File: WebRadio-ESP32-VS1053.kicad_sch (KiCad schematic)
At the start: 75 parts, among them J1 Conn_01x02, J2 JST PH 2mm, J3 JST PH 2mm, J4 AudioJack3, J5 Conn_01x02_Pin, J6 JST PH 2mm, P1 USB_C_Plug_USB2.0, SW1 SW_Push, SW2 SW_Push, SW3 SW_Push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

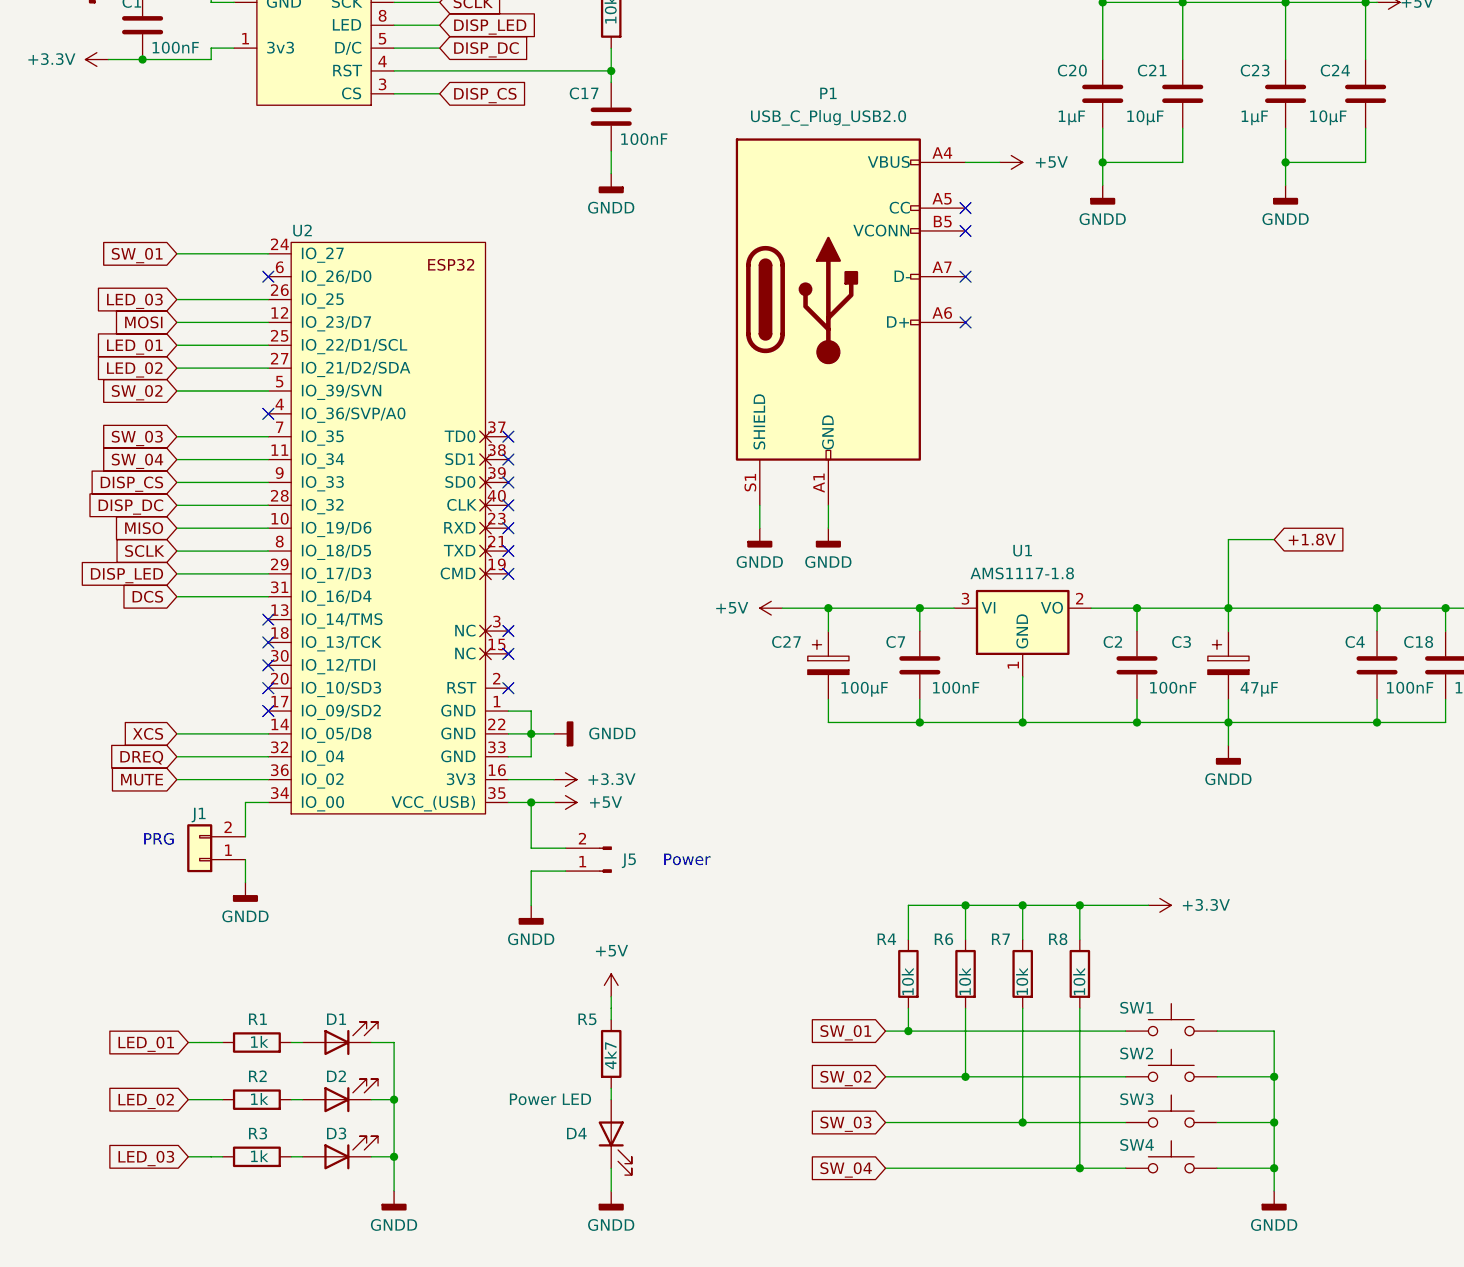
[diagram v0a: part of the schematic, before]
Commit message: add pin header for leds and swiches
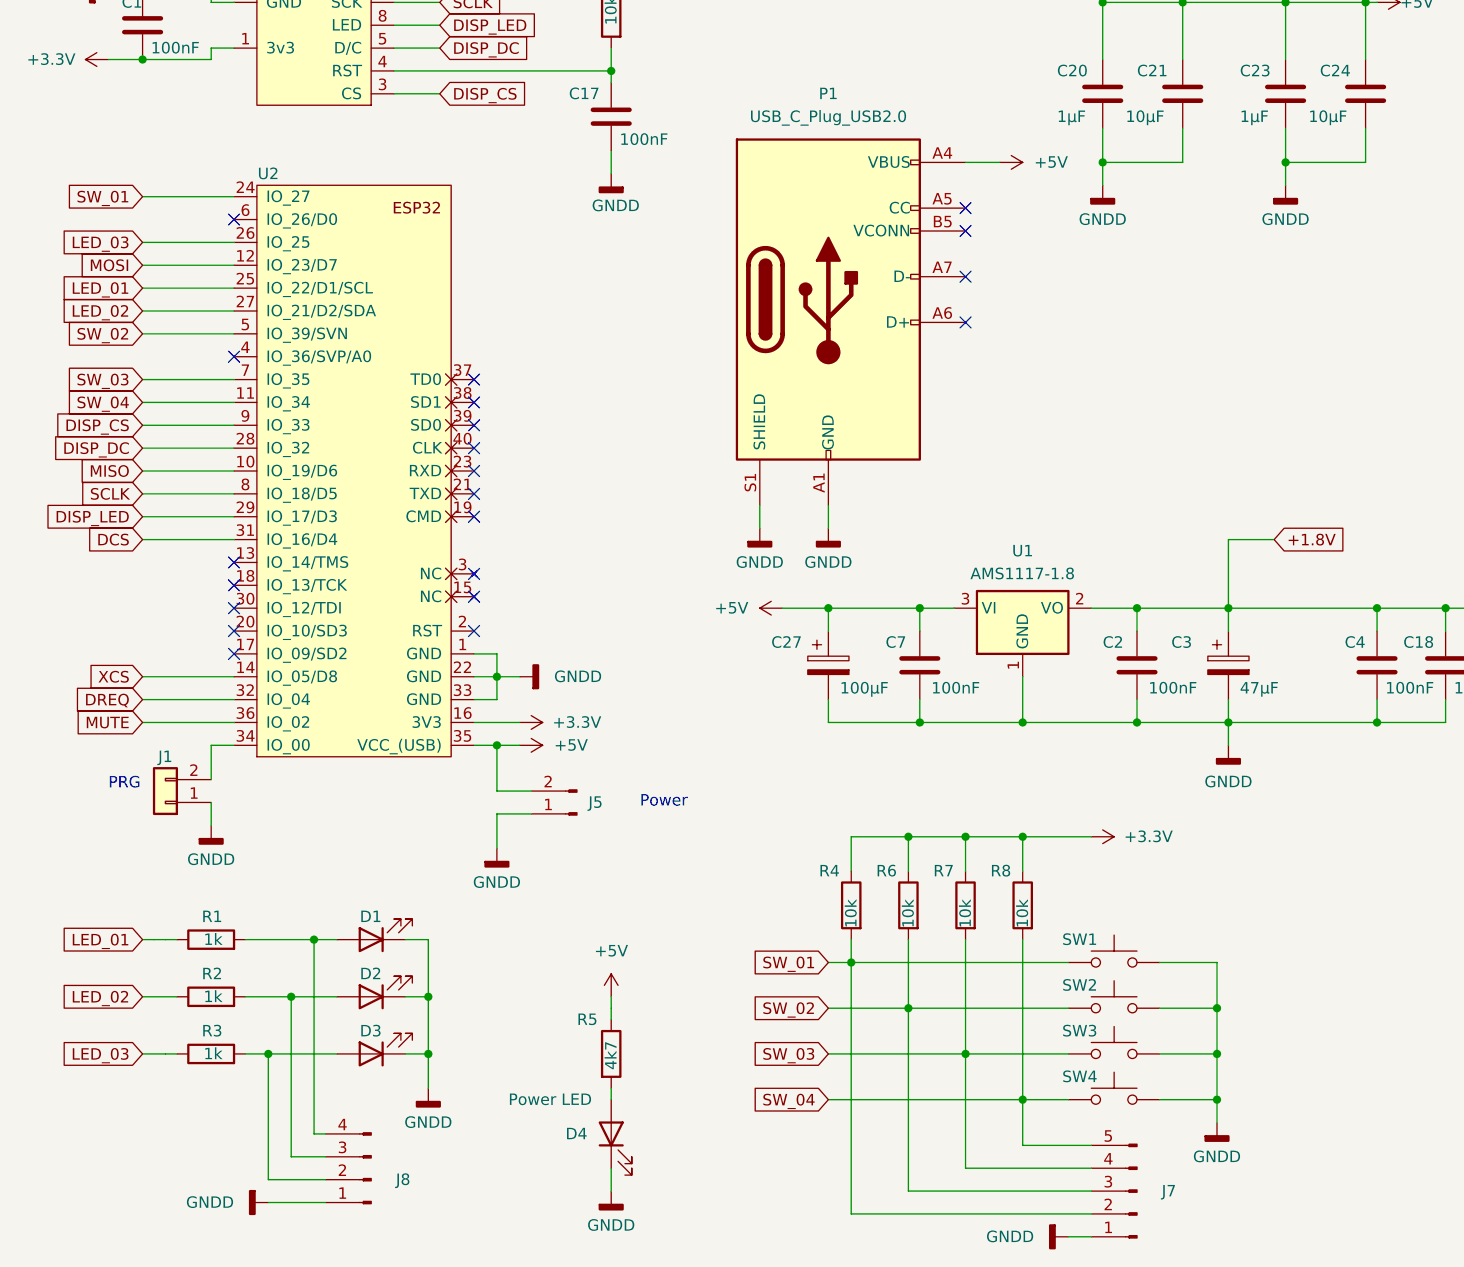
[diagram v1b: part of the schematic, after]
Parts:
- added J7: Conn_01x05_Pin, Connector_PinHeader_2.54mm:PinHeader_1x05_P2.54mm_Vertical, symbol Connector:Conn_01x05_Pin
- added J8: Conn_01x04_Pin, Connector_PinHeader_2.54mm:PinHeader_1x04_P2.54mm_Vertical, symbol Connector:Conn_01x04_Pin
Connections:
- net GNDD: now also J7.1 (Pin_1), J8.1 (Pin_1)
- net SW_01: now also J7.2 (Pin_2)
- net SW_02: now also J7.3 (Pin_3)
- net SW_03: now also J7.4 (Pin_4)
- net SW_04: now also J7.5 (Pin_5)
- net at D3.2 (A), R3.2: now also J8.2 (Pin_2)
- net at D2.2 (A), R2.2: now also J8.3 (Pin_3)
- net at D1.2 (A), R1.2: now also J8.4 (Pin_4)
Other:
- moved on the sheet: D1, D2, D3, J1, J5, R1, R2, R3, R4, R6, R7, R8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

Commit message: include JST PH connectors
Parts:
- removed J5: Conn_01x02_Pin, Connector_JST:JST_PH_S2B-PH-K_1x02_P2.00mm_Horizontal, symbol Library:Conn_01x02_Pin
- removed J7: Conn_01x05_Pin, Connector_PinHeader_2.54mm:PinHeader_1x05_P2.54mm_Vertical, symbol Connector:Conn_01x05_Pin
- removed J8: Conn_01x04_Pin, Connector_PinHeader_2.54mm:PinHeader_1x04_P2.54mm_Vertical, symbol Connector:Conn_01x04_Pin
- added J7: JST PH 2mm, Connector_JST:JST_PH_B2B-PH-K_1x02_P2.00mm_Vertical, symbol Connector_Generic:Conn_01x02
- added J8: Conn_01x05, Connector_JST:JST_PH_B5B-PH-K_1x05_P2.00mm_Vertical, symbol Connector_Generic:Conn_01x05
- added J9: Conn_01x04, Connector_JST:JST_PH_B4B-PH-K_1x04_P2.00mm_Vertical, symbol Connector_Generic:Conn_01x04
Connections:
- net +5V: now also J7.2 (Pin_2)
- net GNDD: now also J7.1 (Pin_1), J8.1 (Pin_1), J9.1 (Pin_1)
- net SW_01: now also J8.2 (Pin_2)
- net SW_02: now also J8.3 (Pin_3)
- net SW_03: now also J8.4 (Pin_4)
- net SW_04: now also J8.5 (Pin_5)
- net at D3.2 (A), R3.2: now also J9.2 (Pin_2)
- net LEFT: now reaches J4.R, J6.3 (Pin_3), R11.2, R12.1, U4.46 (LEFT)
- net at D2.2 (A), R2.2: now also J9.3 (Pin_3)
- net RIGHT: now reaches J4.T, J6.1 (Pin_1), R10.2, R13.1, U4.39 (RIGHT)
- net GBUF: now reaches J4.S, J6.2 (Pin_2), R15.1, U4.42 (GBUF)
- net at D1.2 (A), R1.2: now also J9.4 (Pin_4)
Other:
- moved on the sheet: C1, C17, DS2, P1, R23

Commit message: change some silkscreen data
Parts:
- C27, C3: footprint Capacitor_SMD_AKL:CP_Elec_5x5.7 -> Capacitor_SMD:CP_Elec_5x5.4
- DS2: footprint psch:TFT2.2_SPI_4P_SD -> lib_psch:TFT2.2_SPI_5P_SD
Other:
- note added: "Headphone"
- moved on the sheet: C14, C15, C17, C2, C20, C21, C22, C23, C24, C25, C26, C27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
